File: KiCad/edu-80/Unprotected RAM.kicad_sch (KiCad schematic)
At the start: 8 parts, among them U32 2111A, U33 2111A, U34 2111A, U35 2111A, U36 2111A, U37 2111A, U38 2111A, U39 2111A

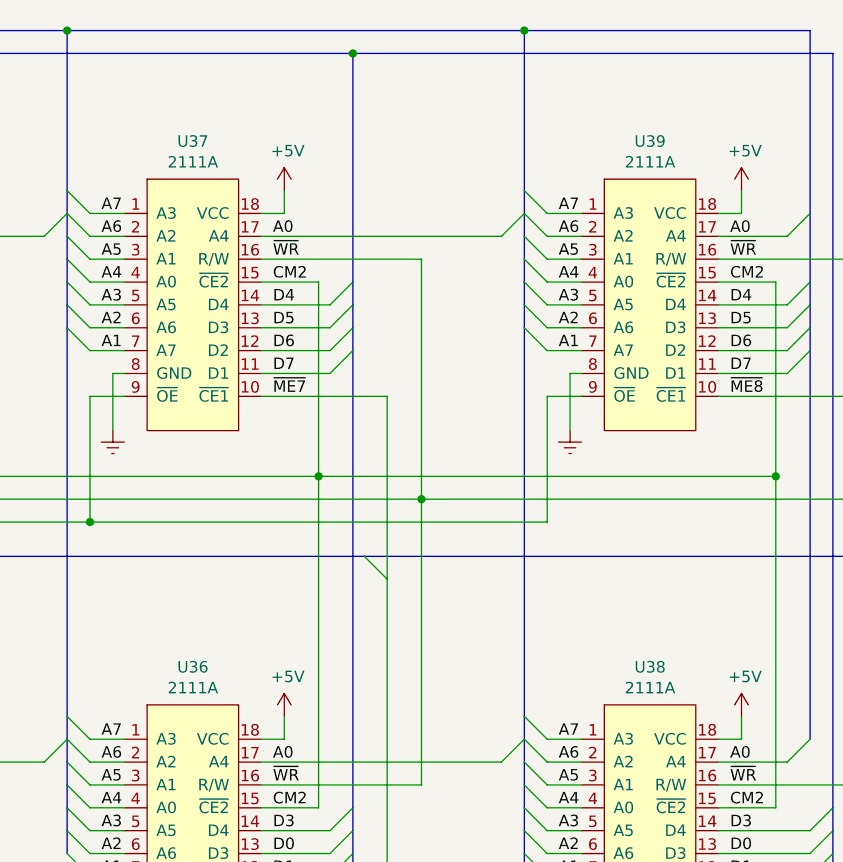
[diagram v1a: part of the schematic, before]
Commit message: Cleaning up the PAL-003 decoding, adding Modifications page.
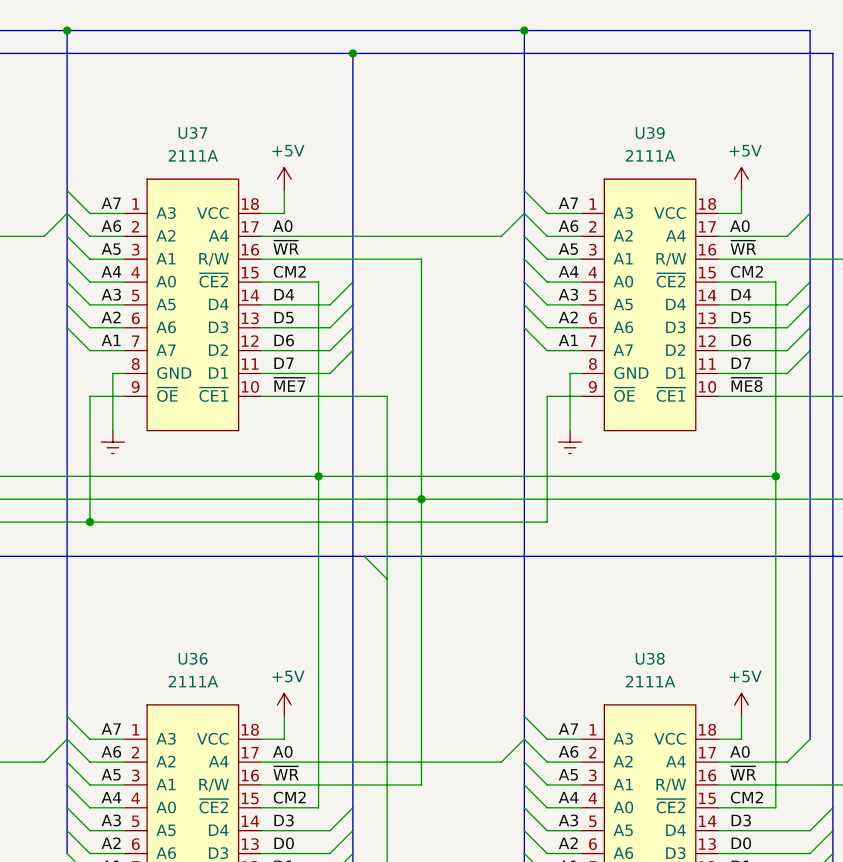
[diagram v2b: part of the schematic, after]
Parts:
- removed U32, U36, U37, U38, U39: 2111A, Package_DIP:DIP-20_W7.62mm, symbol edu-80-rescue:2111A-Edu-80_Symbol
- added U32, U36, U37, U38, U39: 2111A, Package_DIP:DIP-20_W7.62mm, symbol Edu-80_Symbols:2111A
- U33, U34, U35: symbol edu-80-rescue:2111A-Edu-80_Symbol -> Edu-80_Symbols:2111A
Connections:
- net +5V: now also U32.18 (VCC), U36.18 (VCC), U37.18 (VCC), U38.18 (VCC), U39.18 (VCC)
- net A0: now also U32.17 (A4), U36.17 (A4), U37.17 (A4), U38.17 (A4), U39.17 (A4)
- net A1: now also U32.7 (A7), U36.7 (A7), U37.7 (A7), U38.7 (A7), U39.7 (A7)
- net A2: now also U32.6 (A6), U36.6 (A6), U37.6 (A6), U38.6 (A6), U39.6 (A6)
- net A3: now also U32.5 (A5), U36.5 (A5), U37.5 (A5), U38.5 (A5), U39.5 (A5)
- net A4: now also U32.4 (A0), U36.4 (A0), U37.4 (A0), U38.4 (A0), U39.4 (A0)
- net A5: now also U32.3 (A1), U36.3 (A1), U37.3 (A1), U38.3 (A1), U39.3 (A1)
- net A6: now also U32.2 (A2), U36.2 (A2), U37.2 (A2), U38.2 (A2), U39.2 (A2)
- net A7: now also U32.1 (A3), U36.1 (A3), U37.1 (A3), U38.1 (A3), U39.1 (A3)
- net CM2: now also U32.15 (~{CE2}), U36.15 (~{CE2}), U37.15 (~{CE2}), U38.15 (~{CE2}), U39.15 (~{CE2})
- net D0: now also U32.13 (D3), U36.13 (D3), U38.13 (D3)
- net D1: now also U32.12 (D2), U36.12 (D2), U38.12 (D2)
- net D2: now also U32.11 (D1), U36.11 (D1), U38.11 (D1)
- net D3: now also U32.14 (D4), U36.14 (D4), U38.14 (D4)
- net D4: now also U37.14 (D4), U39.14 (D4)
- net D5: now also U37.13 (D3), U39.13 (D3)
- net D6: now also U37.12 (D2), U39.12 (D2)
- net D7: now also U37.11 (D1), U39.11 (D1)
- net Earth: now also U32.8 (GND), U36.8 (GND), U37.8 (GND), U38.8 (GND), U39.8 (GND)
- net ~{ME5}: now also U32.10 (~{CE1})
- net ~{ME7}: now also U36.10 (~{CE1}), U37.10 (~{CE1})
- net ~{ME8}: now also U38.10 (~{CE1}), U39.10 (~{CE1})
- net ~{RD}: now also U32.9 (~{OE}), U36.9 (~{OE}), U37.9 (~{OE}), U38.9 (~{OE}), U39.9 (~{OE})
- net ~{WR}: now also U32.16 (R/W), U36.16 (R/W), U37.16 (R/W), U38.16 (R/W), U39.16 (R/W)

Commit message: Fixed the last of the EDR warnings/errors, adding footprints
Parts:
- U32, U33, U34, U35, U36, U37, U38, U39: footprint Package_DIP:DIP-20_W7.62mm -> Package_DIP:DIP-18_W7.62mm
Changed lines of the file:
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@@
       (effects (font (size 1.27 1.27)))
     )
-    (property "Footprint" "Package_DIP:DIP-20_W7.62mm" (at 111.76 41.91 0)
+    (property "Footprint" "Package_DIP:DIP-18_W7.62mm" (at 111.76 41.91 0)
       (effects (font (size 1.27 1.27)) hide)
     )
@@
       (effects (font (size 1.27 1.27)))
     )
-    (property "Footprint" "Package_DIP:DIP-20_W7.62mm" (at 160.02 41.91 0)
+    (property "Footprint" "Package_DIP:DIP-18_W7.62mm" (at 160.02 41.91 0)
       (effects (font (size 1.27 1.27)) hide)
     )
@@
       (effects (font (size 1.27 1.27)))
     )
-    (property "Footprint" "Package_DIP:DIP-20_W7.62mm" (at 210.82 100.33 0)
+    (property "Footprint" "Package_DIP:DIP-18_W7.62mm" (at 210.82 100.33 0)
       (effects (font (size 1.27 1.27)) hide)
     )
@@
       (effects (font (size 1.27 1.27)))
     )
-    (property "Footprint" "Package_DIP:DIP-20_W7.62mm" (at 111.76 100.33 0)
+    (property "Footprint" "Package_DIP:DIP-18_W7.62mm" (at 111.76 100.33 0)
       (effects (font (size 1.27 1.27)) hide)
     )
@@
       (effects (font (size 1.27 1.27)))
     )
-    (property "Footprint" "Package_DIP:DIP-20_W7.62mm" (at 160.02 100.33 0)
+    (property "Footprint" "Package_DIP:DIP-18_W7.62mm" (at 160.02 100.33 0)
       (effects (font (size 1.27 1.27)) hide)
     )
@@
       (effects (font (size 1.27 1.27)))
     )
-    (property "Footprint" "Package_DIP:DIP-20_W7.62mm" (at 210.82 41.91 0)
+    (property "Footprint" "Package_DIP:DIP-18_W7.62mm" (at 210.82 41.91 0)
       (effects (font (size 1.27 1.27)) hide)
     )
@@
       (effects (font (size 1.27 1.27)))
     )
-    (property "Footprint" "Package_DIP:DIP-20_W7.62mm" (at 60.96 41.91 0)
+    (property "Footprint" "Package_DIP:DIP-18_W7.62mm" (at 60.96 41.91 0)
       (effects (font (size 1.27 1.27)) hide)
     )
@@
       (effects (font (size 1.27 1.27)))
     )
-    (property "Footprint" "Package_DIP:DIP-20_W7.62mm" (at 60.96 100.33 0)
-      (effects (font (size 1.27 1.27)) hide)
-    )
+    (property "Footprint" "Package_DIP:DIP-18_W7.62mm" (at 60.96 100.33 0)
+      (effects (font (size 1.27 1.27)) hide)
+    )
